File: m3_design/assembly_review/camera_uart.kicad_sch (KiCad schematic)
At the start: 13 parts, among them U12 TXU0202DCUR, U13 TPS70933DBVR

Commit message: M3-ASSY-R8: re-placed layout with planned-bus routing, owner-accepted deviations
R8 keeps R7's circuit, RF strip and CH1 pyro block (copied rigidly and
hash-asserted) and re-places everything else: U1 rotated so its free
pins face the RF strip, each block beside the U1 face it talks to, input
protection back at J1, and a fresh deterministic build (r8_build.sh)
with planned-bus routing, no autorouter and no patch stages.

Against R7: signal track 3.36 m -> 1.50 m, signal vias 217 -> 55,
simplicity index 100 -> 15.3, gate exceptions 74 -> 3, hard routing-rule
instances 10 -> 1, 7.7 A neck rise 38/30/44 -> 17.6/14.8/22.3 C,
unreferenced critical samples 27.9 % -> 11.1 %, non-pyro nets within
3 mm of armed copper 23 -> 7.

- Gate: check_r8 (pin contract from pin_table.tsv, F10 separation,
  battery/pyro clearance, loader-pin rule, rigid hashes), route_check
  profile r8, scorecard, dc_solve --necks, reference_audit, paste_check
- Review: passes 2, 3 and 4 found 0 Critical / 0 Major in all eight
  dimensions; pass 5 re-checked the final board (routing, planes,
  integrity) with 0 Critical / 0 Major
- Owner accepted the R8 deviation list on 2026-10-20, including the C10
  vibration item and the listed agent decisions

Board SHA-256 cc044ea0922ff826df19af9d9726d92c096ab2b127025b55d123d8772e5fb4a7.
tools/check.sh: DRC 0, unconnected 0, parity 0, ERC 0; audit, silk,
R8 contract, routing hygiene (0 failing, 3 allowlisted), actuator
contract and fit OK. Before ordering: consign U4, JLC tab acceptance,
cost/stock run within 24 h.

Co-Authored-By: Claude Opus 5.5 <noreply@anthropic.com>
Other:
- note added: "R8: PE8/pin38 UART7_TX and PE7/pin37 UART7_RX use AF7, no flow control (never AF7 on PE9 or PE10); off the ROM loader's USART3. PA7/pin31 controls OE as GPIO."
- note removed: "PB10/pin46 USART3_TX and PB11/pin47 USART3_RX use AF7. PC13/pin7 controls OE as GPIO."
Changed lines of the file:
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@@
 		(title "09 | Camera UART, separate supply domains")
 		(date "2026-10-12")
-		(rev "M3-ASSY-R7")
+		(rev "M3-ASSY-R8")
 		(company "Single-board M3 candidate; full system incomplete"))
 	(text "09 | Camera UART, separate supply domains"
@@
 			(justify right))
 )
-	(text "PB10/pin46 USART3_TX and PB11/pin47 USART3_RX use AF7. PC13/pin7 controls OE as GPIO."
+	(text "R8: PE8/pin38 UART7_TX and PE7/pin37 UART7_RX use AF7, no flow control (never AF7 on PE9 or PE10); off the ROM loader's USART3. PA7/pin31 controls OE as GPIO."
 		(at 20.32 231.14 0)
 		(effects

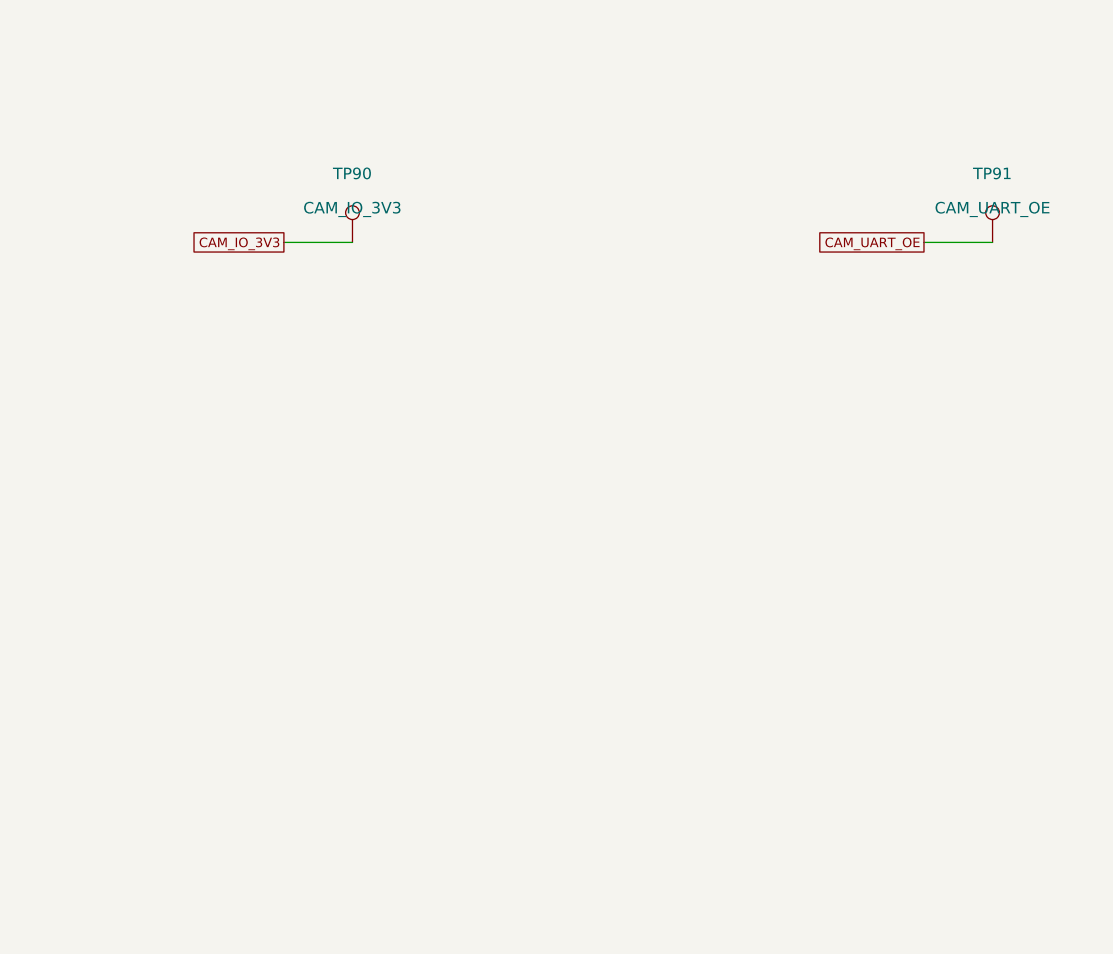
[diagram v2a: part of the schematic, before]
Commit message: R10: m3_design/r10_build.sh and per-family stage gate; m3_design/assembly_review rebuilt as M3-ASSY-R10 (board 883d2db5..., 46 x 90 mm); tools/check.sh passes at zero; binding note bound to the board
Co-Authored-By: Claude Opus 5.5 <noreply@anthropic.com>
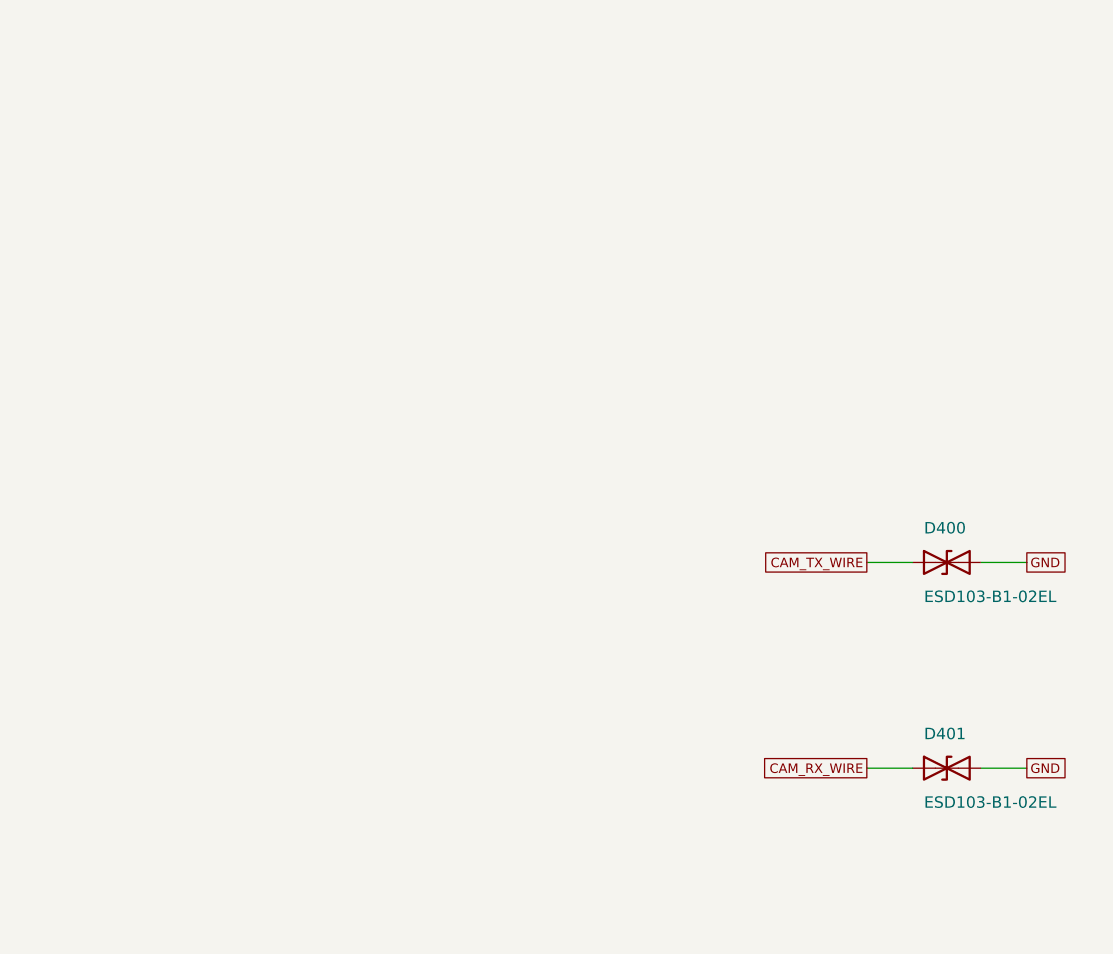
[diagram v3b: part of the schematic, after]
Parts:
- removed TP90: CAM_IO_3V3, rocket:M3_TestPad_1.5, symbol M3:TestPoint
- removed TP91: CAM_UART_OE, rocket:M3_TestPad_1.5, symbol M3:TestPoint
- added D400, D401: ESD103-B1-02EL, rocket:M3_TSLP_2_20, symbol M3:ESD_Bidir
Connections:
- net CAM_RX_WIRE: now also D401.1 (A1)
- net CAM_TX_WIRE: now also D400.1 (A1)
- net GND: now also D400.2 (A2), D401.2 (A2)
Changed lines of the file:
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@@
 		(title "09 | Camera UART, separate supply domains")
 		(date "2026-10-12")
-		(rev "M3-ASSY-R9")
+		(rev "M3-ASSY-R10")
 		(company "Single-board M3 candidate; full system incomplete"))
 	(text "09 | Camera UART, separate supply domains"
@@
 			(justify right))
 )
+	(text "R8: PE8/pin38 UART7_TX and PE7/pin37 UART7_RX use AF7, no flow control (never AF7 on PE9 or PE10); off the ROM loader's USART3. PA7/pin31 controls OE as GPIO."
+		(at 20.32 231.14 0)
+		(effects
+			(font
+				(size 1.05 1.05))
+			(justify left))
+)
+	(text "U12 A-port=MCU3V3. B-port=U13 camera-derived3V3. Never substitute CAM5V for VCCB."
+		(at 20.32 237.48999999999998 0)
+		(effects
+			(font
+				(size 1.05 1.05))
+			(justify left))
+)
+	(text "Reset: R102 holds OE LOW. Set TX idle HIGH before OE; disable OE before power-down."
+		(at 20.32 243.83999999999997 0)
+		(effects
+			(font
+				(size 1.05 1.05))
+			(justify left))
+)
+	(text "U13 EN is internally biased: leave pin3 OPEN, not tied to IN. Pin4 is NC."
+		(at 20.32 250.19 0)
+		(effects
+			(font
+				(size 1.05 1.05))
+			(justify left))
+)
+	(text "UART is 3.3V, not RS232. TXU input operating range0..5.5V is not a cable battery-short rating."
+		(at 20.32 256.53999999999996 0)
+		(effects
+			(font
+				(size 1.05 1.05))
+			(justify left))
+)
+	(text "Camera VIH/VIL/VOH/VOL and timing remain unmeasured. Verify at TP75/76/90 before qualification."
+		(at 20.32 262.89 0)
+		(effects
+			(font
+				(size 1.05 1.05))
+			(justify left))
+)
+	(text "Existing v0.2 bench firmware keeps camera OFF and does not operate this UART. Full system incomplete."
+		(at 20.32 269.24 0)
+		(effects
+			(font
+				(size 1.05 1.05))
+			(justify left))
+)
 	(symbol
-		(lib_id "M3:TestPoint")
-		(at 264.16 193.04 0)
+		(lib_id "M3:ESD_Bidir")
+		(at 330.2 228.6 0)
 		(unit 1)
-		(in_bom no)
+		(in_bom yes)
 		(on_board yes)
 		(dnp no)
-		(property "Reference" "TP90"
-			(at 264.16 185.42 0)
-			(effects
-				(font
-					(size 1.27 1.27))))
-		(property "Value" "CAM_IO_3V3"
-			(at 264.16 189.23 0)
-			(effects
-				(font
-					(size 1.27 1.27))))
-		(property "Footprint" "rocket:M3_TestPad_1.5"
-			(at 264.16 193.04 0)
-			(hide yes)
-			(effects
-				(font
-					(size 1.27 1.27))))
-		(property "Datasheet" ""
-			(at 264.16 193.04 0)
-			(hide yes)
-			(effects
-				(font
-					(size 1.27 1.27))))
-		(property "LCSC" ""
-			(at 264.16 193.04 0)
-			(hide yes)
-			(effects
-				(font
-					(size 1.27 1.27))))
+		(property "Reference" "D400"
+			(at 327.66 224.79 0)
+			(effects
+				(font
+					(size 1.27 1.27))
+				(justify left)))
+		(property "Value" "ESD103-B1-02EL"
+			(at 327.66 232.41 0)
+			(effects
+				(font
+					(size 1.27 1.27))
+				(justify left)))
+		(property "Footprint" "rocket:M3_TSLP_2_20"
+			(at 330.2 228.6 0)
+			(hide yes)
+			(effects
+				(font
+					(size 1.27 1.27))
+				(justify left)))
+		(property "Datasheet" "https://datasheet.lcsc.com/datasheet/pdf/9f837311bec7e3ead15a9d62fb0575b0.pdf?productCode=C535146"
+			(at 330.2 228.6 0)
+			(hide yes)
+			(effects
+				(font
+					(size 1.27 1.27))
+				(justify left)))
+		(property "LCSC" "C535146"
+			(at 330.2 228.6 0)
+			(hide yes)
+			(effects
+				(font
+					(size 1.27 1.27))
+				(justify left)))
+		(property "Manufacturer" "Infineon Technologies"
+			(at 330.2 228.6 0)
+			(hide yes)
+			(effects
+				(font
+					(size 1.27 1.27))
+				(justify left)))
+		(property "Manufacturer Part" "ESD103-B1-02EL E6327"
+			(at 330.2 228.6 0)
+			(hide yes)
+			(effects
+				(font
+					(size 1.27 1.27))
+				(justify left)))
 		(instances
 			(project "m3"
 				(path "/6007a7db-6a58-5660-8beb-956dea045ff8/3918f78b-b8e6-50fb-8165-8fdc93a836ab"
-					(reference "TP90")
+					(reference "D400")
 					(unit 1)))))
 	(wire
 		(pts
-			(xy 264.16 193.04)
-			(xy 256.54 193.04))
-		(stroke
-			(width 0)
-			(type default))
-)
-	(global_label "CAM_IO_3V3"
-		(shape passive)
-		(at 256.54 193.04 0)
-		(effects
-			(font
-				(size 1.05 1.05))
-			(justify right))
+			(xy 326.39 228.6)
+			(xy 321.31 228.6))
+		(stroke
+			(width 0)
+			(type default))
+)
+	(global_label "CAM_TX_WIRE"
+		(shape passive)
+		(at 321.31 228.6 0)
+		(effects
+			(font
+				(size 1.05 1.05))
+			(justify right))
+)
+	(wire
+		(pts
+			(xy 334.01 228.6)
+			(xy 339.09 228.6))
+		(stroke
+			(width 0)
+			(type default))
+)
+	(global_label "GND"
+		(shape passive)
+		(at 339.09 228.6 180)
+		(effects
+			(font
+				(size 1.05 1.05))
+			(justify left))
 )
 	(symbol
-		(lib_id "M3:TestPoint")
-		(at 335.28 193.04 0)
+		(lib_id "M3:ESD_Bidir")
+		(at 330.2 251.46 0)
 		(unit 1)
-		(in_bom no)
+		(in_bom yes)
 		(on_board yes)
 		(dnp no)
-		(property "Reference" "TP91"
-			(at 335.28 185.42 0)
-			(effects
-				(font
-					(size 1.27 1.27))))
-		(property "Value" "CAM_UART_OE"
-			(at 335.28 189.23 0)
-			(effects
-				(font
-					(size 1.27 1.27))))
-		(property "Footprint" "rocket:M3_TestPad_1.5"
-			(at 335.28 193.04 0)
-			(hide yes)
-			(effects
-				(font
-					(size 1.27 1.27))))
-		(property "Datasheet" ""
-			(at 335.28 193.04 0)
-			(hide yes)
-			(effects
-				(font
-					(size 1.27 1.27))))
-		(property "LCSC" ""
-			(at 335.28 193.04 0)
-			(hide yes)
-			(effects
-				(font
-					(size 1.27 1.27))))
+		(property "Reference" "D401"
+			(at 327.66 247.65 0)
+			(effects
+				(font
+					(size 1.27 1.27))
+				(justify left)))
+		(property "Value" "ESD103-B1-02EL"
+			(at 327.66 255.27 0)
+			(effects
+				(font
+					(size 1.27 1.27))
+				(justify left)))
+		(property "Footprint" "rocket:M3_TSLP_2_20"
+			(at 330.2 251.46 0)
+			(hide yes)
+			(effects
+				(font
+					(size 1.27 1.27))
+				(justify left)))
+		(property "Datasheet" "https://datasheet.lcsc.com/datasheet/pdf/9f837311bec7e3ead15a9d62fb0575b0.pdf?productCode=C535146"
+			(at 330.2 251.46 0)
+			(hide yes)
+			(effects
+				(font
+					(size 1.27 1.27))
+				(justify left)))
+		(property "LCSC" "C535146"
+			(at 330.2 251.46 0)
+			(hide yes)
+			(effects
+				(font
+					(size 1.27 1.27))
+				(justify left)))
+		(property "Manufacturer" "Infineon Technologies"
+			(at 330.2 251.46 0)
+			(hide yes)
+			(effects
+				(font
+					(size 1.27 1.27))
+				(justify left)))
+		(property "Manufacturer Part" "ESD103-B1-02EL E6327"
+			(at 330.2 251.46 0)
+			(hide yes)
+			(effects
+				(font
+					(size 1.27 1.27))
+				(justify left)))
 		(instances
 			(project "m3"
 				(path "/6007a7db-6a58-5660-8beb-956dea045ff8/3918f78b-b8e6-50fb-8165-8fdc93a836ab"
-					(reference "TP91")
+					(reference "D401")
 					(unit 1)))))
 	(wire
 		(pts
-			(xy 335.28 193.04)
-			(xy 327.65999999999997 193.04))
-		(stroke
-			(width 0)
-			(type default))
-)
-	(global_label "CAM_UART_OE"
-		(shape passive)
-		(at 327.65999999999997 193.04 0)
-		(effects
-			(font
-				(size 1.05 1.05))
-			(justify right))
-)
-	(text "R8: PE8/pin38 UART7_TX and PE7/pin37 UART7_RX use AF7, no flow control (never AF7 on PE9 or PE10); off the ROM loader's USART3. PA7/pin31 controls OE as GPIO."
-		(at 20.32 231.14 0)
-		(effects
-			(font
-				(size 1.05 1.05))
-			(justify left))
-)
-	(text "U12 A-port=MCU3V3. B-port=U13 camera-derived3V3. Never substitute CAM5V for VCCB."
-		(at 20.32 237.48999999999998 0)
-		(effects
-			(font
-				(size 1.05 1.05))
-			(justify left))
-)
-	(text "Reset: R102 holds OE LOW. Set TX idle HIGH before OE; disable OE before power-down."
-		(at 20.32 243.83999999999997 0)
-		(effects
-			(font
-				(size 1.05 1.05))
-			(justify left))
-)
-	(text "U13 EN is internally biased: leave pin3 OPEN, not tied to IN. Pin4 is NC."
-		(at 20.32 250.19 0)
-		(effects
-			(font
-				(size 1.05 1.05))
-			(justify left))
-)
-	(text "UART is 3.3V, not RS232. TXU input operating range0..5.5V is not a cable battery-short rating."
-		(at 20.32 256.53999999999996 0)
-		(effects
-			(font
-				(size 1.05 1.05))
-			(justify left))
-)
-	(text "Camera VIH/VIL/VOH/VOL and timing remain unmeasured. Verify at TP75/76/90 before qualification."
-		(at 20.32 262.89 0)
-		(effects
-			(font
-				(size 1.05 1.05))
-			(justify left))
-)
-	(text "Existing v0.2 bench firmware keeps camera OFF and does not operate this UART. Full system incomplete."
-		(at 20.32 269.24 0)
-		(effects
-			(font
+			(xy 326.39 251.46)
+			(xy 321.31 251.46))
+		(stroke
+			(width 0)
+			(type default))
+)
+	(global_label "CAM_RX_WIRE"
+		(shape passive)
+		(at 321.31 251.46 0)
+		(effects
+			(font
+				(size 1.05 1.05))
+			(justify right))
+)
+	(wire
+		(pts
+			(xy 334.01 251.46)
+			(xy 339.09 251.46))
+		(stroke
+			(width 0)
+			(type default))
+)
+	(global_label "GND"
+		(shape passive)
+		(at 339.09 251.46 180)
+		(effects
+			(font
